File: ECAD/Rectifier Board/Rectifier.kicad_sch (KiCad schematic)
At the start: 70 parts, among them J1 MAINS, Q1 IXFH48N60X3, U2 IR1153S

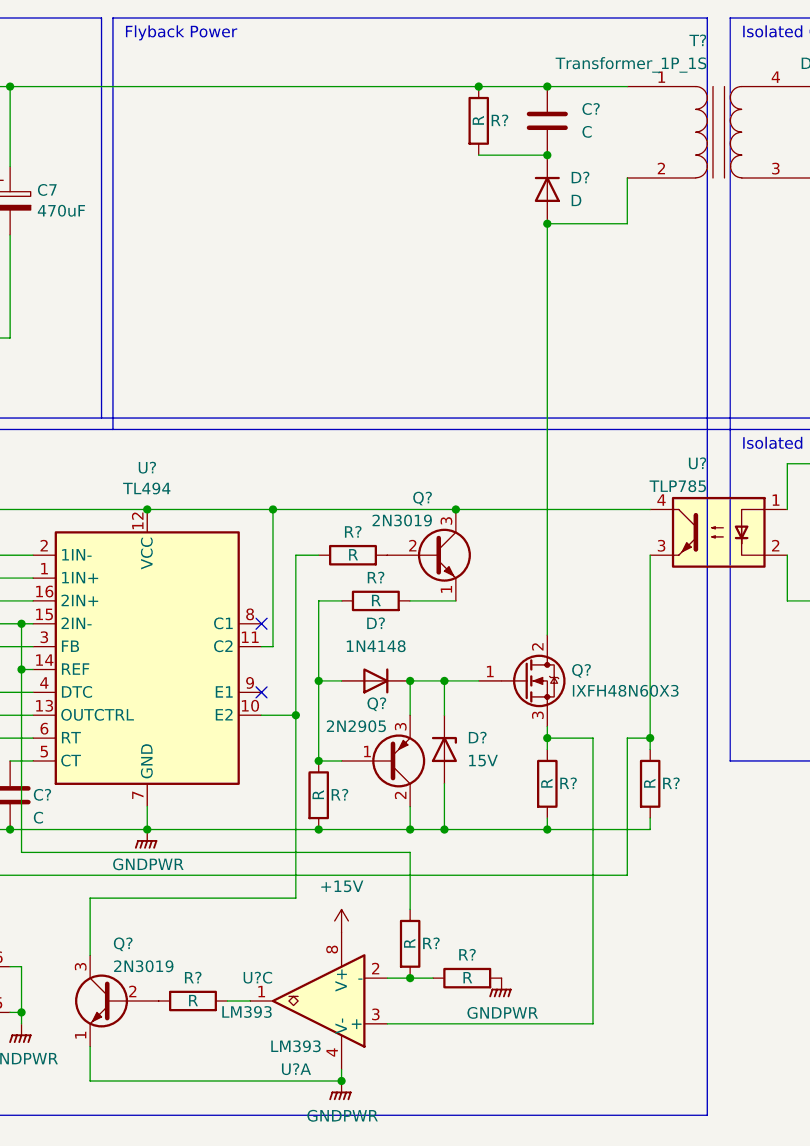
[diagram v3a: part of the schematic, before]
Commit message: add some component values
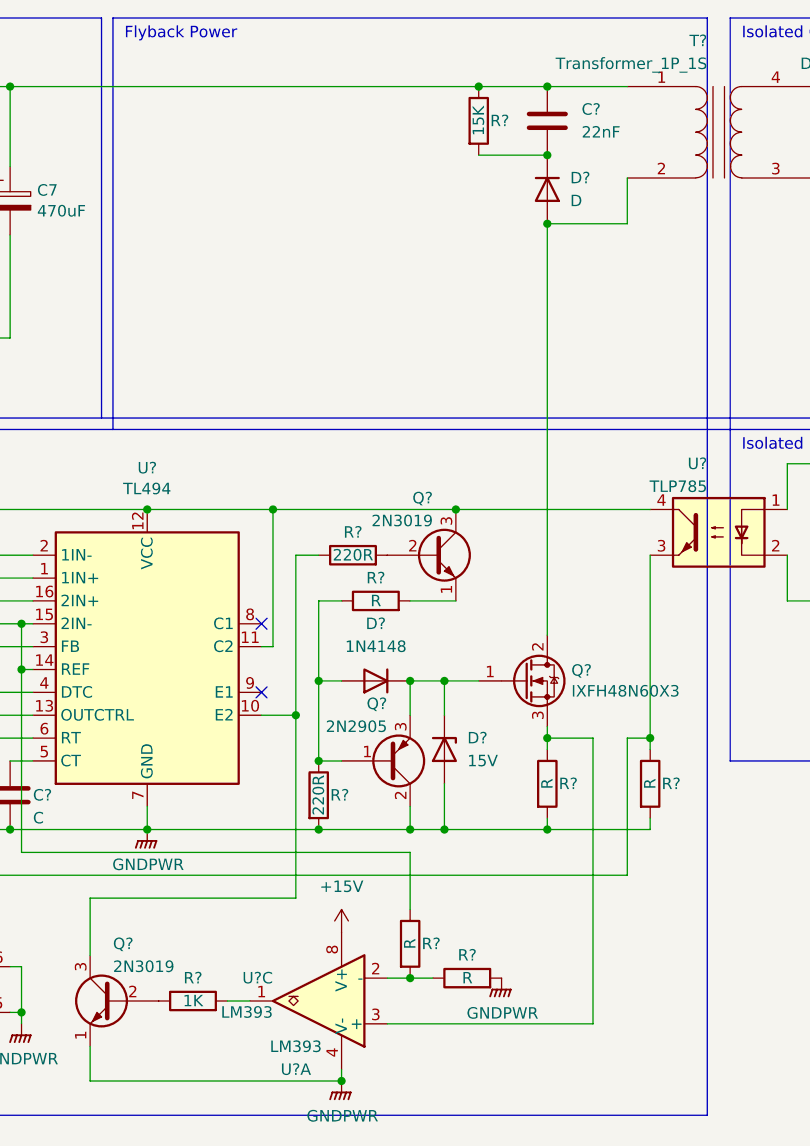
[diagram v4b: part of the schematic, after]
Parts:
- C?: value C -> 22nF
- R?: value R -> 1K
- R? (x2): value R -> 220R
- R?: value R -> 15K
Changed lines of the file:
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@@
       (effects (font (size 1.27 1.27)) (justify left))
     )
-    (property "Value" "C" (id 1) (at 243.84 29.2099 0)
+    (property "Value" "22nF" (id 1) (at 243.84 29.2099 0)
       (effects (font (size 1.27 1.27)) (justify left))
     )
@@
     (in_bom yes) (on_board yes)
     (property "Reference" "R?" (id 0) (at 200.66 123.19 90))
-    (property "Value" "R" (id 1) (at 200.66 125.73 90))
+    (property "Value" "1K" (id 1) (at 200.66 125.73 90))
     (property "Footprint" "" (id 2) (at 200.66 127.508 90)
       (effects (font (size 1.27 1.27)) hide)
@@
       (effects (font (size 1.27 1.27)) (justify left))
     )
-    (property "Value" "R" (id 1) (at 214.63 102.87 90))
+    (property "Value" "220R" (id 1) (at 214.63 102.87 90))
     (property "Footprint" "" (id 2) (at 212.852 102.87 90)
       (effects (font (size 1.27 1.27)) hide)
@@
       (effects (font (size 1.27 1.27)) (justify left))
     )
-    (property "Value" "R" (id 1) (at 232.41 27.94 90))
+    (property "Value" "15K" (id 1) (at 232.41 27.94 90))
     (property "Footprint" "" (id 2) (at 230.632 27.94 90)
       (effects (font (size 1.27 1.27)) hide)
@@
     (in_bom yes) (on_board yes)
     (property "Reference" "R?" (id 0) (at 218.44 73.66 90))
-    (property "Value" "R" (id 1) (at 218.44 76.2 90))
+    (property "Value" "220R" (id 1) (at 218.44 76.2 90))
     (property "Footprint" "" (id 2) (at 218.44 77.978 90)
       (effects (font (size 1.27 1.27)) hide)
@@
     )
     (path "/549764ec-3882-407d-9220-ed9d42854e74"
-      (reference "C?") (unit 1) (value "C") (footprint "")
+      (reference "C?") (unit 1) (value "22nF") (footprint "")
     )
     (path "/58d3a54e-57ff-46ab-8139-a031c1949b45"
@@
     )
     (path "/7b945a2a-77e0-4fb7-8bbc-c87bcae38960"
-      (reference "R?") (unit 1) (value "R") (footprint "")
+      (reference "R?") (unit 1) (value "1K") (footprint "")
     )
     (path "/7e801041-5a0e-42d2-9687-326e2f6e485a"
@@
     )
     (path "/9c3f7b92-20b4-4aba-9c2a-6718ee5c5f88"
-      (reference "R?") (unit 1) (value "R") (footprint "")
+      (reference "R?") (unit 1) (value "220R") (footprint "")
     )
     (path "/9fd9c4af-b403-47fb-b51e-b25bcc9a98c1"
@@
     )
     (path "/a605dbc4-418f-4613-ae05-cb9a6dc046cd"
-      (reference "R?") (unit 1) (value "R") (footprint "")
+      (reference "R?") (unit 1) (value "15K") (footprint "")
     )
     (path "/b2b83193-b314-4d08-af2d-a2d87b4b0937"
@@
     )
     (path "/df0a206c-ee22-4525-bc4b-b25f9de4e2a1"
-      (reference "R?") (unit 1) (value "R") (footprint "")
+      (reference "R?") (unit 1) (value "220R") (footprint "")
     )
     (path "/e652a55e-43e8-4f27-9dc8-5d1f2784c251"

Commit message: select parts
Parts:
- D2: value D_Schottky -> MBRF1060CL
- D?: value D -> 1N4007
- D?: value D_Schottky -> V30DM60CL
- R?: value R -> 10R
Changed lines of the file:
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@@
     (stroke (width 0) (type default) (color 0 0 0 0))
   )
-  (polyline (pts (xy 147.32 60.96) (xy 147.32 106.68))
+  (polyline (pts (xy 147.32 60.96) (xy 147.32 105.41))
     (stroke (width 0) (type default) (color 0 0 0 0))
   )
@@
     (stroke (width 0) (type default) (color 0 0 0 0))
   )
-  (polyline (pts (xy 147.32 106.68) (xy 76.2 105.41))
+  (polyline (pts (xy 147.32 105.41) (xy 76.2 105.41))
     (stroke (width 0) (type default) (color 0 0 0 0))
   )
@@
     (in_bom yes) (on_board yes)
     (property "Reference" "D2" (id 0) (at 139.7 18.6182 0))
-    (property "Value" "D_Schottky" (id 1) (at 139.7 20.9296 0))
+    (property "Value" "MBRF1060CL" (id 1) (at 139.7 20.9296 0))
     (property "Footprint" "" (id 2) (at 139.7 24.13 0)
       (effects (font (size 1.27 1.27)) hide)
@@
       (effects (font (size 1.27 1.27)) (justify left))
     )
-    (property "Value" "D" (id 1) (at 242.57 36.8299 90)
+    (property "Value" "1N4007" (id 1) (at 242.57 36.8299 90)
       (effects (font (size 1.27 1.27)) (justify left))
     )
@@
     (in_bom yes) (on_board yes)
     (property "Reference" "D?" (id 0) (at 273.05 26.67 0))
-    (property "Value" "D_Schottky" (id 1) (at 273.05 21.59 0))
+    (property "Value" "V30DM60CL" (id 1) (at 273.05 21.59 0))
     (property "Footprint" "" (id 2) (at 273.05 24.13 0)
       (effects (font (size 1.27 1.27)) hide)
@@
     (in_bom yes) (on_board yes)
     (property "Reference" "R?" (id 0) (at 220.98 78.74 90))
-    (property "Value" "R" (id 1) (at 220.98 81.28 90))
+    (property "Value" "10R" (id 1) (at 220.98 81.28 90))
     (property "Footprint" "" (id 2) (at 220.98 83.058 90)
       (effects (font (size 1.27 1.27)) hide)
@@
     )
     (path "/00000000-0000-0000-0000-00006210839a"
-      (reference "D2") (unit 1) (value "D_Schottky") (footprint "")
+      (reference "D2") (unit 1) (value "MBRF1060CL") (footprint "")
     )
     (path "/075edbe9-3ea3-4759-a5c3-a899d46fc9fd"
-      (reference "D?") (unit 1) (value "D") (footprint "")
+      (reference "D?") (unit 1) (value "1N4007") (footprint "")
     )
     (path "/0bbda886-a0b4-4a97-949c-66ccc1a57444"
@@
     )
     (path "/58a7b2a5-650b-451b-8d27-f4fdc5c9e59c"
-      (reference "D?") (unit 1) (value "D_Schottky") (footprint "")
+      (reference "D?") (unit 1) (value "V30DM60CL") (footprint "")
     )
     (path "/bc475c18-5d54-4009-aa03-20d77b331bf0"
@@
     )
     (path "/da75c9b2-bcab-48b4-8ac4-a253b3c71074"
-      (reference "R?") (unit 1) (value "R") (footprint "")
+      (reference "R?") (unit 1) (value "10R") (footprint "")
     )
     (path "/df0a206c-ee22-4525-bc4b-b25f9de4e2a1"
